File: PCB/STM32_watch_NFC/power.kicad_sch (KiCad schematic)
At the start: 26 parts, among them J2 USB_C_Receptacle_PowerOnly_6P, U2 MIC5365-3.3YC5, U4 MT3608

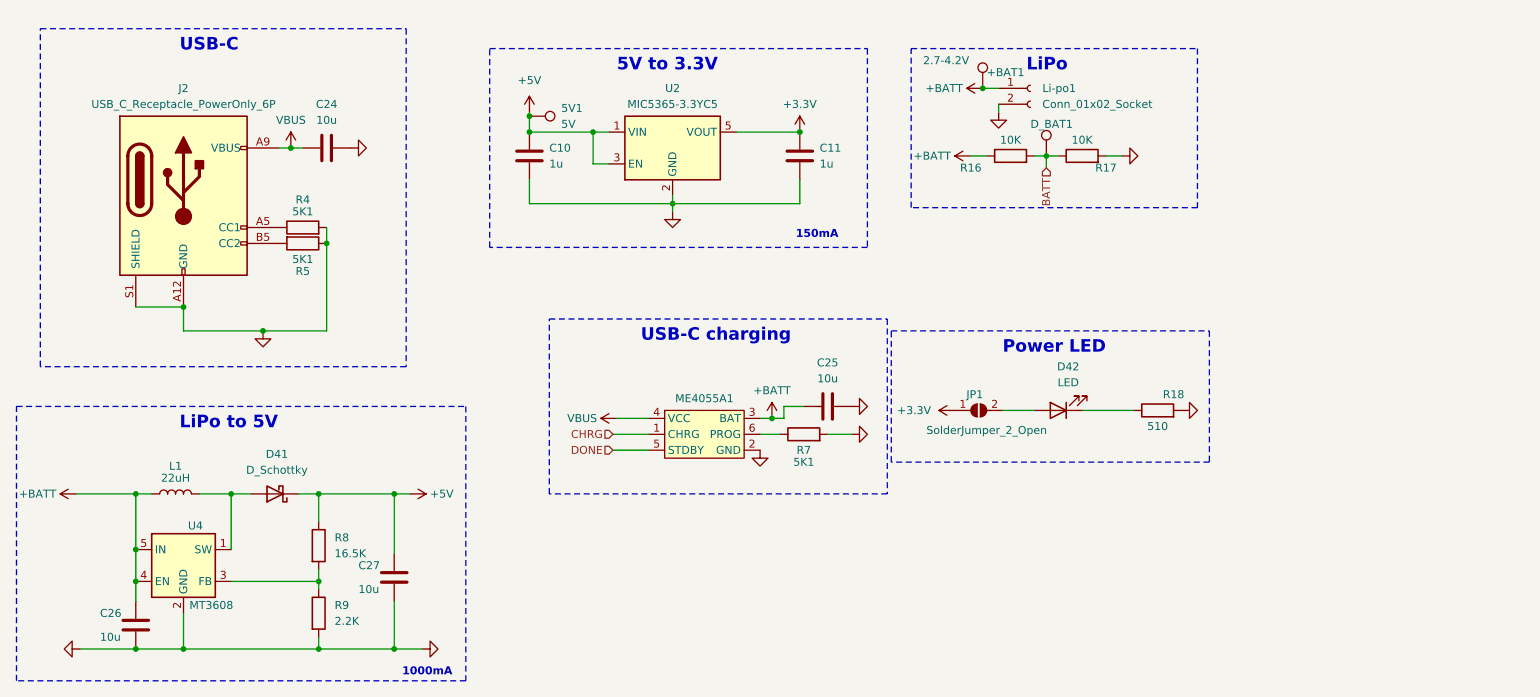
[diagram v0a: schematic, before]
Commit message: Kicad - new Routing 4.5
NEW 7-segment display + connection, new charger, charging status
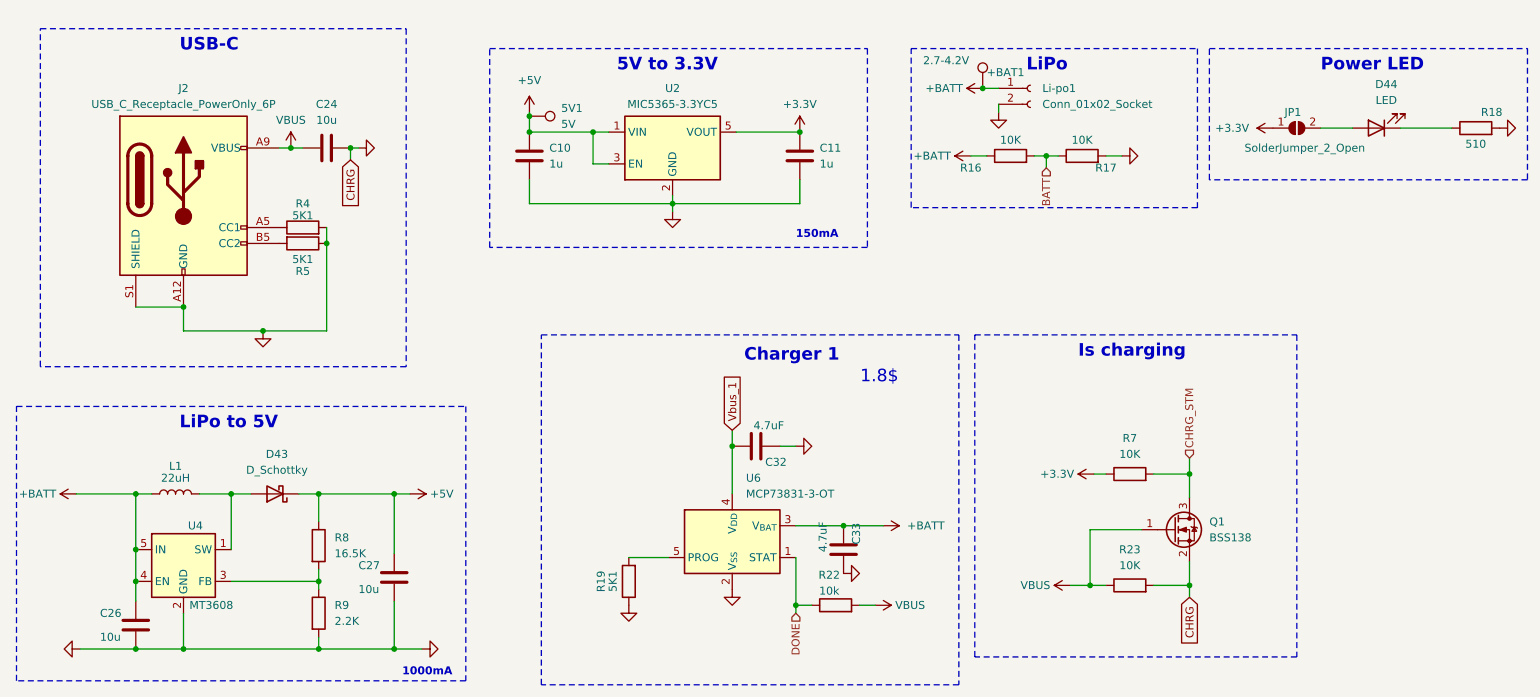
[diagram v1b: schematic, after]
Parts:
- removed C25: 10u, Capacitor_SMD:C_0603_1608Metric, symbol Device:C
- removed D_BAT1: ~, TestPoint:TestPoint_Pad_D1.0mm, symbol Connector:TestPoint
- removed ME4055A1: ~, Package_TO_SOT_SMD:SOT-23-6, symbol Power:ME4055AM6G
- added C32, C33: 4.7uF, Capacitor_SMD:C_0603_1608Metric, symbol Device:C
- added Q1: BSS138, Package_TO_SOT_SMD:SOT-23, symbol Transistor_FET:BSS138
- added R19: 5K1, Resistor_SMD:R_0402_1005Metric, symbol Device:R
- added R22: 10k, Resistor_SMD:R_0603_1608Metric, symbol Device:R
- added R23: 10K, Resistor_SMD:R_0402_1005Metric, symbol Device:R
- added U6: MCP73831-3-OT, Package_TO_SOT_SMD:SOT-23-5, symbol Battery_Management:MCP73831-3-OT
- R7: value 5K1 -> 10K; LCSC C284599 -> C308028
- renumbered D41 to D43, D42 to D44
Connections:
- net +3.3V: now also R7.1
- net +BATT: now also C33.2, U6.3 (V_{BAT})
- net DONE: now also R22.1, U6.1 (STAT)
- net GND: now also C32.2, C33.1, Q1.2 (S), R19.1, R23.2, U6.2 (V_{SS}); no longer R7.2
- net VBUS: now also Q1.1 (G), R22.2, R23.1
- new net: R19.2, U6.5 (PROG)
- new net CHRG_STM: Q1.3 (D), R7.2
- new net Vbus_1: C32.1, U6.4 (V_{DD})
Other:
- note added: "1.8$"
- note added: "Charger 1"
- note added: "Is charging"
- note removed: "USB-C charging"
- moved on the sheet: D44, JP1, R18

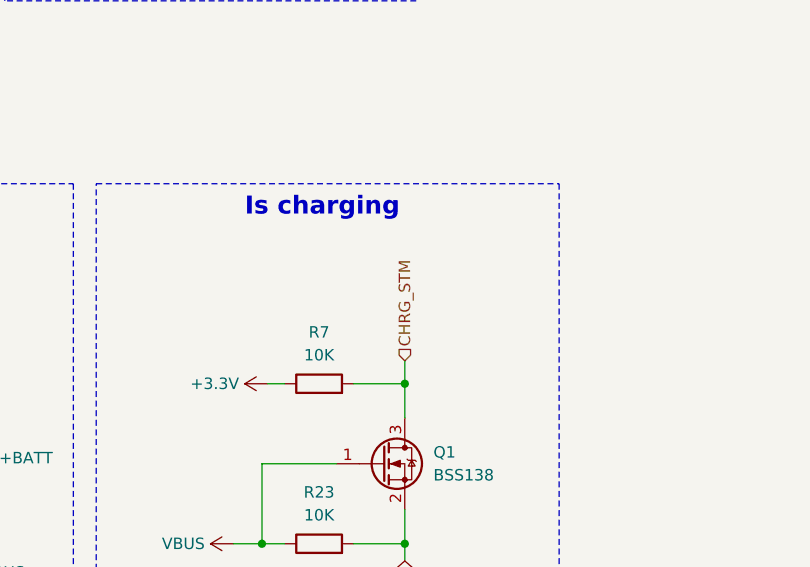
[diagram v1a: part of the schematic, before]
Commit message: Kicad/STM - new Routing 5
All STM32 peripherals connected, new firmware file + new code in it :)
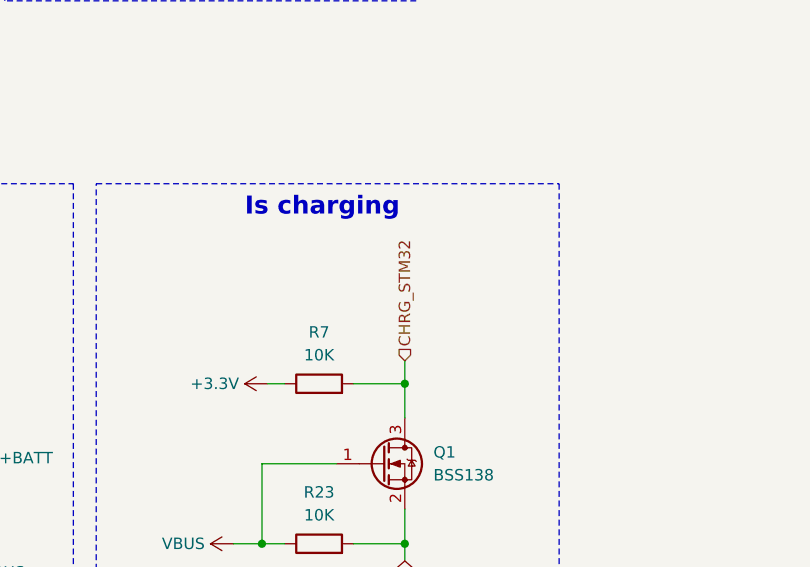
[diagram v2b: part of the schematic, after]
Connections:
- net CHRG_STM renamed CHRG_STM32
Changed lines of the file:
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@@
 		)
 	)
-	(hierarchical_label "CHRG_STM"
+	(hierarchical_label "CHRG_STM32"
 		(shape input)
 		(at 210.82 89.535 90)

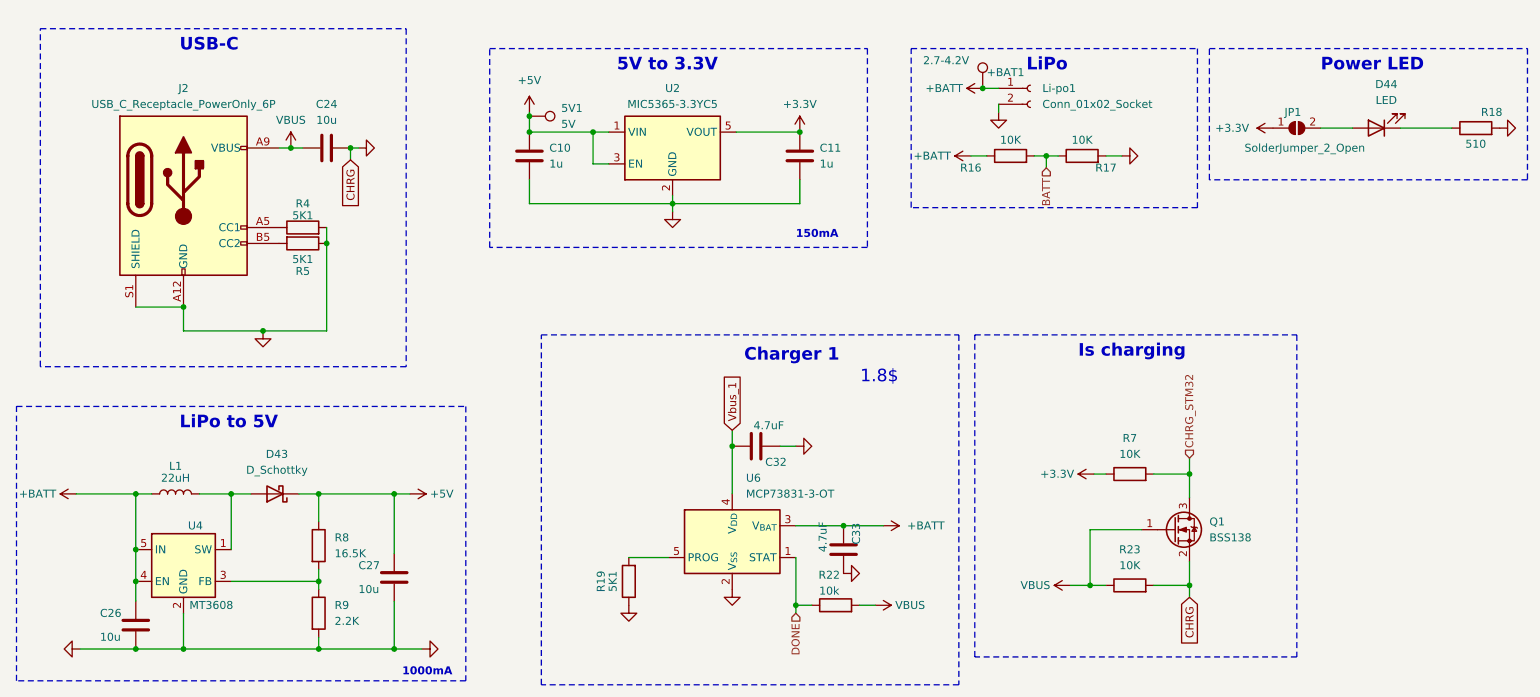
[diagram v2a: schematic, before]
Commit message: TM1637 - in next commit I will delete the driver and connect the leds directly through matrix
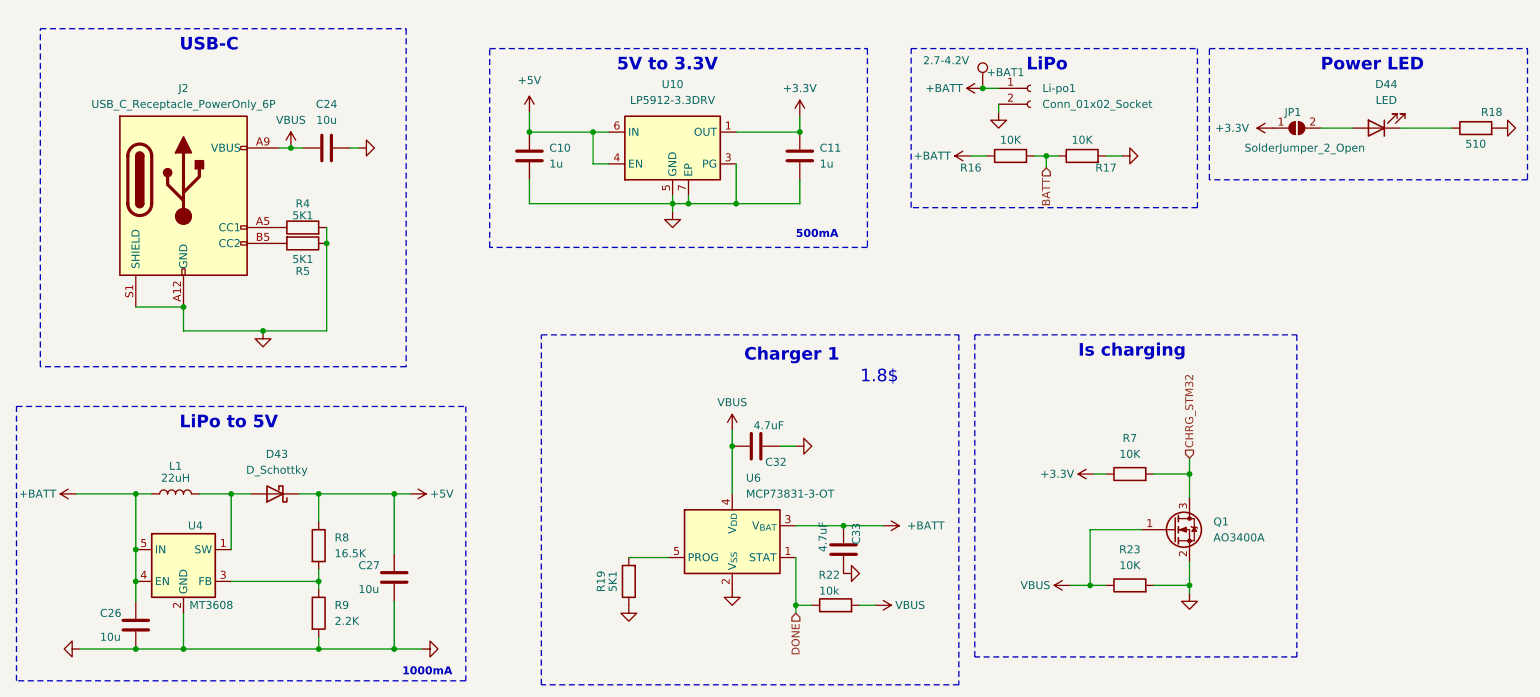
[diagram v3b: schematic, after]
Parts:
- removed 5V1: 5V, TestPoint:TestPoint_Pad_D1.5mm, symbol Connector:TestPoint
- removed Q1: BSS138, Package_TO_SOT_SMD:SOT-23, symbol Transistor_FET:BSS138
- removed U2: MIC5365-3.3YC5, Package_TO_SOT_SMD:SOT-353_SC-70-5, symbol Regulator_Linear:MIC5365-3.3YC5
- added Q1: AO3400A, Package_TO_SOT_SMD:SOT-23, symbol Transistor_FET:AO3400A
- added U10: LP5912-3.3DRV, Package_SON:WSON-6-1EP_2x2mm_P0.65mm_EP1x1.6mm_ThermalVias, symbol Regulator_Linear:LP5912-3.3DRV
- L1: footprint Components:SLW3015 -> Inductor_SMD:L_Sunlord_SWPA3015S; LCSC C206322 -> C167761
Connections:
- net Vbus_1 is gone; now on net VBUS: C32.1, U6.4 (V_{DD})
- net +3.3V: now also U10.1 (OUT)
- net +5V: now also U10.4 (EN), U10.6 (IN)
- net CHRG_STM32: now also Q1.3 (D)
- net GND: now also Q1.2 (S), U10.3 (PG), U10.5 (GND), U10.7 (EP)
- net VBUS: now also Q1.1 (G)
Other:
- note added: "500mA"
- note removed: "150mA"

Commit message: Kicad/STM - new Routing 6
Version before Boston to work on it there - needs to replace every component :(
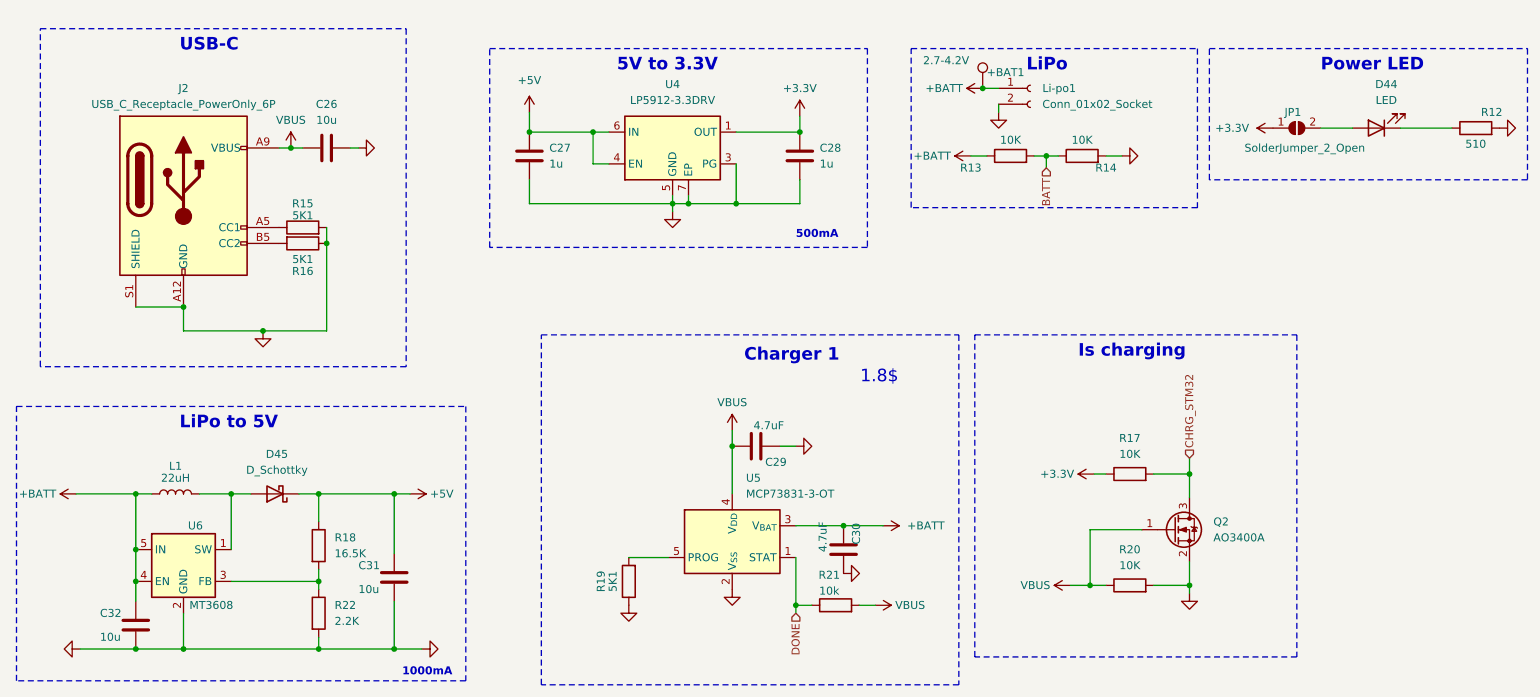
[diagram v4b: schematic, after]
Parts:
- U4: renamed from U10; footprint Package_SON:WSON-6-1EP_2x2mm_P0.65mm_EP1x1.6mm_ThermalVias -> Package_SON:WSON-6-1EP_2x2mm_P0.65mm_EP1x1.6mm
- renumbered C24 to C26, C10 to C27, C11 to C28, C32 to C29, C33 to C30, C27 to C31, C26 to C32, D43 to D45, Q1 to Q2, R18 to R12, R16 to R13, R17 to R14, R4 to R15, R5 to R16, R7 to R17, R8 to R18, R23 to R20, R22 to R21, R9 to R22, U6 to U5, U4 to U6

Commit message: Component placement
I placed every component in logical way
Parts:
- removed D44: LED, LED_SMD:LED_0603_1608Metric, symbol Device:LED
- removed JP1: SolderJumper_2_Open, Jumper:SolderJumper-2_P1.3mm_Open_TrianglePad1.0x1.5mm, symbol Jumper:SolderJumper_2_Open
- removed R12: 510, Resistor_SMD:R_0402_1005Metric, symbol Device:R
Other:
- note removed: "Power LED"

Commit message: Routing #3
Done with routing - meet with DennyBrambor and teaching him how to route :)
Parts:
- C26, C31, C32: LCSC C77040 -> C19702
- C27, C28: LCSC C412453 -> C52923
- C29, C30: LCSC C1705 -> C19666
- D45: LCSC C145179 -> C727120
- R13, R14, R17, R20: LCSC C308028 -> C25744
- R15, R16: LCSC C284599 -> C25905
- R21: footprint Resistor_SMD:R_0603_1608Metric -> Resistor_SMD:R_0402_1005Metric; LCSC C25804 -> C25744
- R22: LCSC C509322 -> C25879
- U4: LCSC (none) -> C524780
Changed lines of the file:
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@@
 			)
 		)
-		(property "LCSC" "C509322"
+		(property "LCSC" "C25879"
 			(at 71.755 114.3 0)
 			(effects
@@
 			)
 		)
-		(property "LCSC" "C412453"
+		(property "LCSC" "C52923"
 			(at 105.41 41.275 0)
 			(effects
@@
 			)
 		)
-		(property "LCSC" "C308028"
+		(property "LCSC" "C25744"
 			(at 201.295 109.855 90)
 			(effects
@@
 			)
 		)
+		(property "LCSC" "C524780"
+			(at 128.27 40.005 0)
+			(effects
+				(font
+					(size 1.27 1.27)
+				)
+				(hide yes)
+			)
+		)
 		(pin "5"
 		)
@@
 			)
 		)
-		(property "LCSC" "C77040"
+		(property "LCSC" "C19702"
 			(at 42.545 116.205 0)
 			(effects
@@
 			)
 		)
-		(property "LCSC" "C77040"
+		(property "LCSC" "C19702"
 			(at 83.82 108.585 0)
 			(effects
@@
 			)
 		)
-		(property "LCSC" "C284599"
+		(property "LCSC" "C25905"
 			(at 69.215 55.245 90)
 			(effects
@@
 			)
 		)
-		(property "Footprint" "Resistor_SMD:R_0603_1608Metric"
+		(property "Footprint" "Resistor_SMD:R_0402_1005Metric"
 			(at 154.305 114.808 90)
 			(effects
@@
 			)
 		)
-		(property "LCSC" "C25804"
+		(property "LCSC" "C25744"
 			(at 154.305 113.03 90)
 			(effects
@@
 			)
 		)
-		(property "LCSC" "C145179"
+		(property "LCSC" "C727120"
 			(at 64.77 95.25 0)
 			(effects
@@
 			)
 		)
-		(property "LCSC" "C1705"
+		(property "LCSC" "C19666"
 			(at 155.575 104.14 90)
 			(effects
@@
 			)
 		)
-		(property "LCSC" "C308028"
+		(property "LCSC" "C25744"
 			(at 182.245 41.275 90)
 			(effects
@@
 			)
 		)
-		(property "LCSC" "C308028"
+		(property "LCSC" "C25744"
 			(at 193.675 41.275 90)
 			(effects
@@
 			)
 		)
-		(property "LCSC" "C412453"
+		(property "LCSC" "C52923"
 			(at 148.59 41.275 0)
 			(effects
@@
 			)
 		)
-		(property "LCSC" "C284599"
+		(property "LCSC" "C25905"
 			(at 69.215 52.705 90)
 			(effects
@@
 			)
 		)
-		(property "LCSC" "C77040"
+		(property "LCSC" "C19702"
 			(at 73.025 40.005 90)
 			(effects
@@
 			)
 		)
-		(property "LCSC" "C308028"
+		(property "LCSC" "C25744"
 			(at 201.295 92.075 90)
 			(effects
@@
 			)
 		)
-		(property "LCSC" "C1705"
+		(property "LCSC" "C19666"
 			(at 141.605 87.63 90)
 			(effects

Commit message: Routing #4
Unfortunately I had to change all vias to be 0.45/0.3 so it was a lot of pain :)
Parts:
- Li-po1: footprint Connector_JST:JST_SUR_SM02B-SURS-TF_1x02-1MP_P0.80mm_Horizontal -> Connector_Molex:Molex_Pico-EZmate_78171-0002_1x02-1MP_P1.20mm_Vertical; LCSC C566239 -> C505023
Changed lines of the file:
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@@
 			)
 		)
-		(property "Footprint" "Connector_JST:JST_SUR_SM02B-SURS-TF_1x02-1MP_P0.80mm_Horizontal"
+		(property "Footprint" "Connector_Molex:Molex_Pico-EZmate_78171-0002_1x02-1MP_P1.20mm_Vertical"
 			(at 185.42 30.48 0)
 			(effects
@@
 			)
 		)
-		(property "LCSC" "C566239"
+		(property "LCSC" "C505023"
 			(at 185.42 30.48 0)
 			(effects

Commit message: Revision.B.0
Production folder in panelized_watch was send to production. YAAAH
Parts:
- removed J2: USB_C_Receptacle_PowerOnly_6P, Connector_USB:USB_C_Receptacle_GCT_USB4135-GF-A_6P_TopMnt_Horizontal, symbol Connector:USB_C_Receptacle_PowerOnly_6P
- added J3: USB_C_Receptacle_USB2.0_16P, Connector_USB:USB_C_Receptacle_GCT_USB4110, symbol Connector:USB_C_Receptacle_USB2.0_16P
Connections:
- net GND: now also J3.A1 (GND), J3.A12 (GND), J3.B1 (GND), J3.B12 (GND), J3.S1 (SHIELD)
- net VBUS: now also J3.A4 (VBUS), J3.A9 (VBUS), J3.B4 (VBUS), J3.B9 (VBUS)
- net at R15.1: now also J3.A5 (CC1)
- net at R16.2: now also J3.B5 (CC2)
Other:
- moved on the sheet: C26, R15, R16
